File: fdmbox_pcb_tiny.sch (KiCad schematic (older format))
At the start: 126 parts, among them J1 ICSP, J10 T_E0_IN, J11 T_E1_IN, J12 T_BED_IN, J13 T_ENV_IN, J14 X0_MIN, J15 X1_MIN, J16 Y_MIN, J17 Z_MAX, J18 BLTOUCH, J19 LOADCELL, J2 MOT_E0, J20 RGB0, J21 RGB1, J22 BED_PWM, J23 GP_PWM, J24 FAN_E0_OUT, J25 FAN_E1_OUT, J26 MOT_X0, J27 MOT_X1, J28 MOT_Y0, J29 MOT_Y1, J3 MOT_E1, J30 MOT_Z0, J31 MOT_Z1, J32 POWER_IN, J33 LFAN_E0_OUT, J34 LFAN_E1_OUT, J35 FAN_ENV_OUT, J36 POWER_OUT, J37 T_E0_OUT, J38 T_E1_OUT, J39 RPI_Conn, J4 MOT_SPARE0, J5 MOT_SPARE1, J6 STP_SEL, J7 STP_SEL, J8 STP_SEL, J9 STP_SEL, Q1 BSS138, Q2 STP55NF06L, Q3 STP55NF06L, Q4 STP55NF06L, Q5 STP55NF06L, Q6 STP55NF06L, Q7 BSS138, Q8 BSS138, Q9 BSS138, SW1 RESET, U1 ATmega2560V-8AU, U2 TSR_2-2450, U3 PCA9531-Driver_LED, Y1 16MHz

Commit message: Added connections to MCU
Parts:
- added J23: Z_MAX, symbol Connector_Generic:Conn_01x02
- SW1: symbol fdmbox_pcb-cache:Switch_SW_DIP_x01 -> fdmbox_pcb_tiny-rescue:Switch_SW_DIP_x01-fdmbox_pcb-cache
- U3: symbol fdmbox_pcb-cache:fdmbox_pcb-rescue_PCA9531-Driver_LED -> fdmbox_pcb_tiny-rescue:fdmbox_pcb-rescue_PCA9531-Driver_LED-fdmbox_pcb-cache
- renumbered C4 to C1, C7 to C10, C14 to C11, C8 to C12, C9 to C13, C10 to C14, C5 to C2, C6 to C3, C1 to C4, C11 to C5, C2 to C6, C3 to C7, C12 to C8, C13 to C9, D2 to D1, D3 to D2, D1 to D3, F3 to F1, F4 to F2, F1 to F3, F2 to F4, J32 to J1, J13 to J10, J36 to J11, J7 to J12, J37 to J13, J1 to J14, J14 to J15, J38 to J16, J24 to J17, J15 to J18, J3 to J19, J6 to J2, J16 to J20, J25 to J21, J8 to J22, J17 to J24, J26 to J25, J39 to J26, J18 to J27, J27 to J28, J4 to J29, J10 to J3, J19 to J30, J28 to J31, J9 to J32, J20 to J33, J29 to J34, J21 to J35, J22 to J36, J30 to J37, J5 to J38, J23 to J39, J33 to J4, J31 to J40, J11 to J5, J34 to J6, J12 to J7, J35 to J8, J2 to J9, Q8 to Q1, Q9 to Q2, Q2 to Q3, Q3 to Q4, Q4 to Q5, Q5 to Q6, Q6 to Q7, Q1 to Q8, Q7 to Q9, R13 to R1, R29 to R10, R21 to R11, R25 to R12, R30 to R13, R33 to R14, R41 to R15, R43 to R16, R34 to R17, R36 to R18, R8 to R19, R37 to R2, R14 to R20, R31 to R21, R1 to R22, R32 to R23, R9 to R24, R15 to R25, R22 to R26, R2 to R27, R26 to R28, R10 to R29, R44 to R3, R16 to R30, R3 to R31, R11 to R32, R17 to R33, R23 to R34, R27 to R35, R4 to R36, R12 to R37, R18 to R38, R5 to R39, R38 to R4, R24 to R40, R28 to R41, R7 to R42, R20 to R43, R6 to R44, R19 to R45, R45 to R5, R40 to R6, R39 to R7, R42 to R8, R35 to R9, U2 to U1, U1 to U2
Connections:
- net RGB0_B is gone; now on net LED0_B: J33.3 (Pin_3)
- net RGB0_G is gone; now on net LED0_G: J33.2 (Pin_2)
- net RGB0_R is gone; now on net LED0_R: J33.1 (Pin_1)
- net RGB1_B is gone; now on net LED1_B: J35.3 (Pin_3)
- net RGB1_G is gone; now on net LED1_G: J35.2 (Pin_2)
- net RGB1_R is gone; now on net LED1_R: J35.1 (Pin_1)
- net BEDPWM: now also U2.17 (PH5)
- net BLTOUCH: now also U2.23 (PB4)
- net E0_DIR: now also U2.77 (PA1)
- net E0_EN: now also U2.76 (PA2)
- net E0_STEP: now also U2.78 (PA0)
- net E1_DIR: now also U2.74 (PA4)
- net E1_EN: now also U2.73 (PA5)
- net E1_STEP: now also U2.75 (PA3)
- net F_E0_L: now also U2.18 (PH6)
- net F_E1_L: now also U2.27 (PH7)
- net F_ENV_L: now also U2.6 (PE4)
- net GND: now also J23.2 (Pin_2)
- net GPPWM: now also U2.14 (PH2)
- net LCELL: now also U2.50 (PD7)
- net LF_E0_L: now also U2.4 (PE2)
- net LF_E1_L: now also U2.5 (PE3)
- net MISO: now also U2.22 (PB3)
- net MOSI: now also U2.21 (PB2)
- net MOT_X0_DIR: now also U2.96 (PF1)
- net MOT_X0_EN: now also U2.95 (PF2)
- net MOT_X0_STEP: now also U2.97 (PF0)
- net MOT_X1_DIR: now also U2.93 (PF4)
- net MOT_X1_EN: now also U2.92 (PF5)
- net MOT_X1_STEP: now also U2.94 (PF3)
- net MOT_Y0_DIR: now also U2.54 (PC1)
- net MOT_Y0_EN: now also U2.55 (PC2)
- net MOT_Y0_STEP: now also U2.53 (PC0)
- net MOT_Y1_DIR: now also U2.57 (PC4)
- net MOT_Y1_EN: now also U2.58 (PC5)
- net MOT_Y1_STEP: now also U2.56 (PC3)
- net MOT_Z0_DIR: now also U2.64 (PJ1)
- net MOT_Z0_EN: now also U2.63 (PJ0)
- net MOT_Z0_STEP: now also U2.65 (PJ2)
- net MOT_Z1_DIR: now also U2.67 (PJ4)
- net MOT_Z1_EN: now also U2.66 (PJ3)
- net MOT_Z1_STEP: now also U2.68 (PJ5)
- net RX_5: now also U2.3 (PE1)
- net SCK: now also U2.20 (PB1)
- net SCL: now also U2.43 (PD0)
- net SDA: now also U2.44 (PD1)
- net SPARE0_DIR: now also U2.71 (PA7)
- net SPARE0_EN: now also U2.19 (PB0)
- net SPARE0_STEP: now also U2.72 (PA6)
- net SPARE1_DIR: now also U2.25 (PB6)
- net SPARE1_EN: now also U2.26 (PB7)
- net SPARE1_STEP: now also U2.24 (PB5)
- net TX_5: now also U2.2 (PE0)
- net T_BED_IN: now also U2.88 (PK1)
- net T_E0_L: now also U2.15 (PH3)
- net T_E1_IN: now also U2.87 (PK2); no longer C5.1, J3.1 (Pin_1), R10.2
- net T_E1_L: now also U2.16 (PH4)
- net T_ENV_IN: now also U2.89 (PK0)
- net X0MIN: now also U2.45 (PD2)
- net X1MIN: now also U2.46 (PD3)
- net YMIN: now also U2.47 (PD4)
- net ZMAX: now also U2.49 (PD6)
- net ZMIN: now reaches U2.48 (PD5)
- net ZMIN: now also J23.1 (Pin_1)
- net T_E0_IN: now reaches U2.86 (PK3)
- net T_E0_IN: now also C5.1, J3.1 (Pin_1), R10.2
- no-connect marks 29 -> 58
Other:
- moved on the sheet: C4, C6, C7, D3, J14, J15, J18, J20, SW1

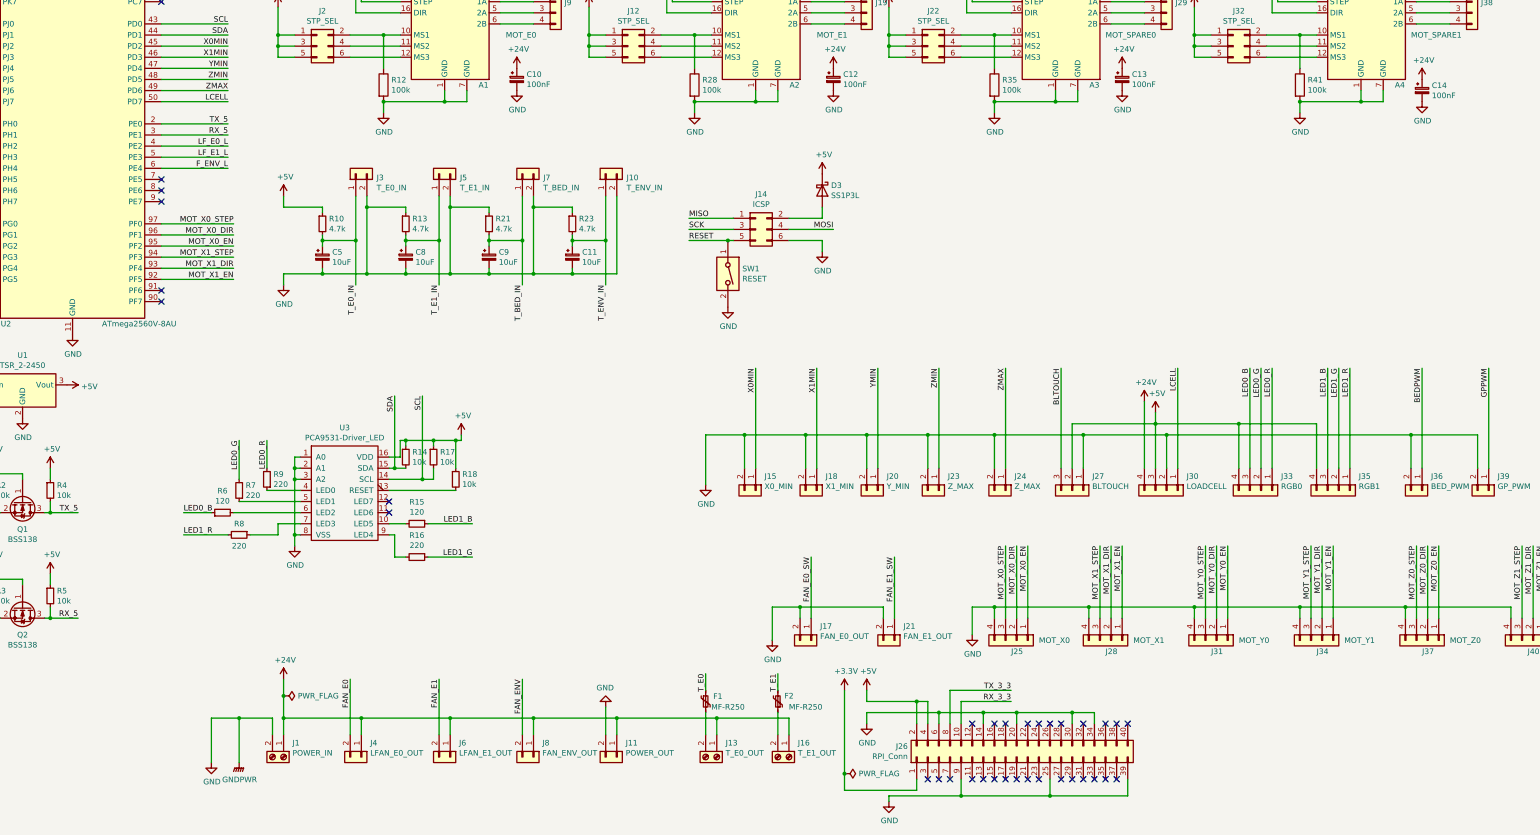
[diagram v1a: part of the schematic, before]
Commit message: added footprints to schematics, started pcb layout
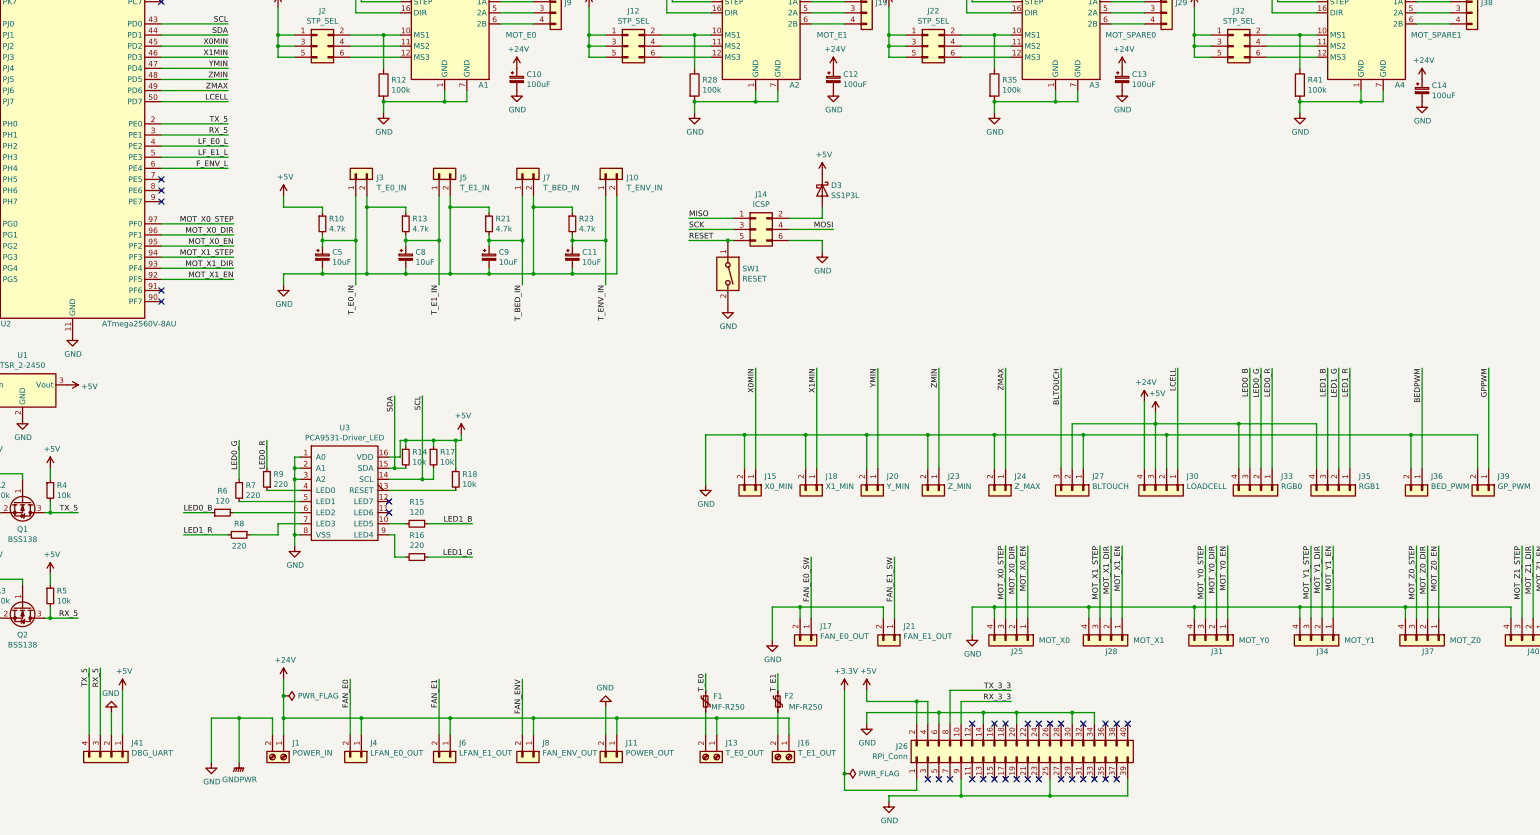
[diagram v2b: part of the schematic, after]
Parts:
- added J41: DBG_UART, Connector_PinSocket_2.54mm:PinSocket_1x04_P2.54mm_Vertical, symbol Connector_Generic:Conn_01x04
- C10, C12, C13, C14: value 100nF -> 100uF; footprint (none) -> Capacitor_SMD:CP_Elec_8x6.2
- C11, C5, C8, C9: footprint (none) -> Capacitor_SMD:CP_Elec_5x5.4
- D3: footprint (none) -> Diode_SMD:DO-220AA
- F1, F2: footprint (none) -> Capacitor_THT:C_Disc_D5.1mm_W3.2mm_P5.00mm
- F3, F4: footprint (none) -> Capacitor_THT:C_Rect_L11.0mm_W5.1mm_P10.00mm_MKT
- J1, J13, J16: footprint (none) -> TerminalBlock_RND:TerminalBlock_RND_205-00287_1x02_P5.08mm_Horizontal
- J10, J11, J15, J17, J18, J20, J21, J24, J3, J36, J39, J4, J5, J6, J7, J8: footprint (none) -> Connector_JST:JST_XH_B02B-XH-AM_1x02_P2.50mm_Vertical
- J19, J25, J28, J29, J30, J31, J33, J34, J35, J37, J38, J40, J9: footprint (none) -> Connector_JST:JST_XH_B04B-XH-AM_1x04_P2.50mm_Vertical
- J23: value Z_MAX -> Z_MIN; footprint (none) -> Connector_JST:JST_XH_B02B-XH-AM_1x02_P2.50mm_Vertical
- J26: footprint (none) -> Connector_PinHeader_2.54mm:PinHeader_2x20_P2.54mm_Vertical
- J27: footprint (none) -> Connector_JST:JST_XH_B03B-XH-AM_1x03_P2.50mm_Vertical
- Q3, Q4, Q5, Q6, Q7: footprint (none) -> Package_TO_SOT_THT:TO-220-3_Vertical
- SW1: footprint (none) -> Button_Switch_THT:SW_Tactile_Straight_KSL0Axx1LFTR
- U3: footprint (none) -> Package_SO:TSSOP-16_4.4x5mm_P0.65mm
- Y1: footprint (none) -> Crystal:Crystal_HC49-U_Vertical
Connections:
- net +5V: now also J41.1 (Pin_1)
- net GND: now also J41.2 (Pin_2)
- net RX_5: now also J41.3 (Pin_3)
- net TX_5: now also J41.4 (Pin_4)

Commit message: PCB finished -so far..
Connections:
- net MOT_Y1_DIR is gone; now on net MOT_Y_DIR: J34.2 (Pin_2), U2.57 (PC4)
- net MOT_Y1_EN is gone; now on net MOT_Y_EN: J34.1 (Pin_1), U2.58 (PC5)
- net MOT_Y1_STEP is gone; now on net MOT_Y_STEP: J34.3 (Pin_3), U2.56 (PC3)
- net +24V: now also J17.2 (Pin_2), J21.2 (Pin_2)
- net +5V: now also J12.2 (Pin_2), J12.4 (Pin_4), J12.6 (Pin_6), J2.2 (Pin_2), J2.4 (Pin_4), J2.6 (Pin_6), J22.2 (Pin_2), J22.4 (Pin_4), J22.6 (Pin_6), J32.2 (Pin_2), J32.4 (Pin_4), J32.6 (Pin_6), R13.1, R21.1, R23.1; no longer J12.1 (Pin_1), J12.3 (Pin_3), J12.5 (Pin_5), J2.1 (Pin_1), J2.3 (Pin_3), J2.5 (Pin_5), J22.1 (Pin_1), J22.3 (Pin_3), J22.5 (Pin_5), J32.1 (Pin_1), J32.3 (Pin_3), J32.5 (Pin_5)
- net BEDPWM: now also U2.14 (PH2); no longer U2.17 (PH5)
- net BLTOUCH: now also U2.46 (PD3); no longer U2.23 (PB4)
- net E0_DIR: now also U2.95 (PF2); no longer U2.77 (PA1)
- net E0_EN: now also U2.97 (PF0); no longer U2.76 (PA2)
- net E0_STEP: now also U2.96 (PF1); no longer U2.78 (PA0)
- net E1_DIR: now also U2.92 (PF5); no longer U2.74 (PA4)
- net E1_EN: now also U2.94 (PF3); no longer U2.73 (PA5)
- net E1_STEP: now also U2.93 (PF4); no longer U2.75 (PA3)
- net F_E0_L: now also U2.15 (PH3); no longer U2.18 (PH6)
- net F_E1_L: now also U2.16 (PH4); no longer U2.27 (PH7)
- net GND: no longer J17.2 (Pin_2), J21.2 (Pin_2), R13.1, R21.1, R23.1
- net GPPWM: now also U2.7 (PE5); no longer U2.14 (PH2)
- net LCELL: now also U2.45 (PD2); no longer U2.50 (PD7)
- net MOT_X0_DIR: now also U2.64 (PJ1); no longer U2.96 (PF1)
- net MOT_X0_EN: now also U2.65 (PJ2); no longer U2.95 (PF2)
- net MOT_X0_STEP: now also U2.63 (PJ0); no longer U2.97 (PF0)
- net MOT_X1_DIR: now also U2.67 (PJ4); no longer U2.93 (PF4)
- net MOT_X1_EN: now also U2.68 (PJ5); no longer U2.92 (PF5)
- net MOT_X1_STEP: now also U2.66 (PJ3); no longer U2.94 (PF3)
- net SPARE0_DIR: now also U2.76 (PA2); no longer U2.71 (PA7)
- net SPARE0_EN: now also U2.78 (PA0); no longer U2.19 (PB0)
- net SPARE0_STEP: now also U2.77 (PA1); no longer U2.72 (PA6)
- net SPARE1_DIR: now also U2.71 (PA7); no longer U2.25 (PB6)
- net SPARE1_EN: now also U2.73 (PA5); no longer U2.26 (PB7)
- net SPARE1_STEP: now also U2.72 (PA6); no longer U2.24 (PB5)
- net T_E0_L: now also U2.17 (PH5); no longer U2.15 (PH3)
- net T_E1_L: now also U2.18 (PH6); no longer U2.16 (PH4)
- net X0MIN: now also U2.47 (PD4); no longer U2.45 (PD2)
- net X1MIN: now also U2.51 (PG0); no longer U2.46 (PD3)
- net YMIN: now also U2.50 (PD7); no longer U2.47 (PD4)
- net ZMAX: now also U2.48 (PD5); no longer U2.49 (PD6)
- net ZMIN: now also U2.49 (PD6); no longer U2.48 (PD5)
- net at A1.10 (MS1), R12.1: now also J2.1 (Pin_1); no longer J2.2 (Pin_2)
- net at A1.11 (MS2): now also J2.3 (Pin_3); no longer J2.4 (Pin_4)
- net at A1.12 (MS3): now also J2.5 (Pin_5); no longer J2.6 (Pin_6)
- net at A2.10 (MS1), R28.1: now also J12.1 (Pin_1); no longer J12.2 (Pin_2)
- net at A2.11 (MS2): now also J12.3 (Pin_3); no longer J12.4 (Pin_4)
- net at A2.12 (MS3): now also J12.5 (Pin_5); no longer J12.6 (Pin_6)
- net at A3.10 (MS1), R35.1: now also J22.1 (Pin_1); no longer J22.2 (Pin_2)
- net at A3.11 (MS2): now also J22.3 (Pin_3); no longer J22.4 (Pin_4)
- net at A3.12 (MS3): now also J22.5 (Pin_5); no longer J22.6 (Pin_6)
- net at A4.10 (MS1), R41.1: now also J32.1 (Pin_1); no longer J32.2 (Pin_2)
- net at A4.11 (MS2): now also J32.3 (Pin_3); no longer J32.4 (Pin_4)
- net at A4.12 (MS3): now also J32.5 (Pin_5); no longer J32.6 (Pin_6)
- net MOT_Y0_DIR renamed MOT_Y_DIR
- net MOT_Y_DIR: no longer U2.54 (PC1)
- net MOT_Y0_EN renamed MOT_Y_EN
- net MOT_Y_EN: no longer U2.55 (PC2)
- net MOT_Y0_STEP renamed MOT_Y_STEP
- net MOT_Y_STEP: no longer U2.53 (PC0)
- net MOT_Z0_DIR renamed MOT_Z_DIR
- net MOT_Z_DIR: now also J40.2 (Pin_2), U2.54 (PC1); no longer U2.64 (PJ1)
- net MOT_Z0_EN renamed MOT_Z_EN
- net MOT_Z_EN: now also J40.1 (Pin_1), U2.55 (PC2); no longer U2.63 (PJ0)
- net MOT_Z0_STEP renamed MOT_Z_STEP
- net MOT_Z_STEP: now also J40.3 (Pin_3), U2.53 (PC0); no longer U2.65 (PJ2)
- removed net MOT_Z1_DIR: J40.2 (Pin_2), U2.67 (PJ4)
- removed net MOT_Z1_EN: J40.1 (Pin_1), U2.66 (PJ3)
- removed net MOT_Z1_STEP: J40.3 (Pin_3), U2.68 (PJ5)
- no-connect marks 58 -> 57
